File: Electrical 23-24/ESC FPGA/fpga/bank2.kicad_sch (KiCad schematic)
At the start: 1 part, among them U1 XC6SLX4-TQG144

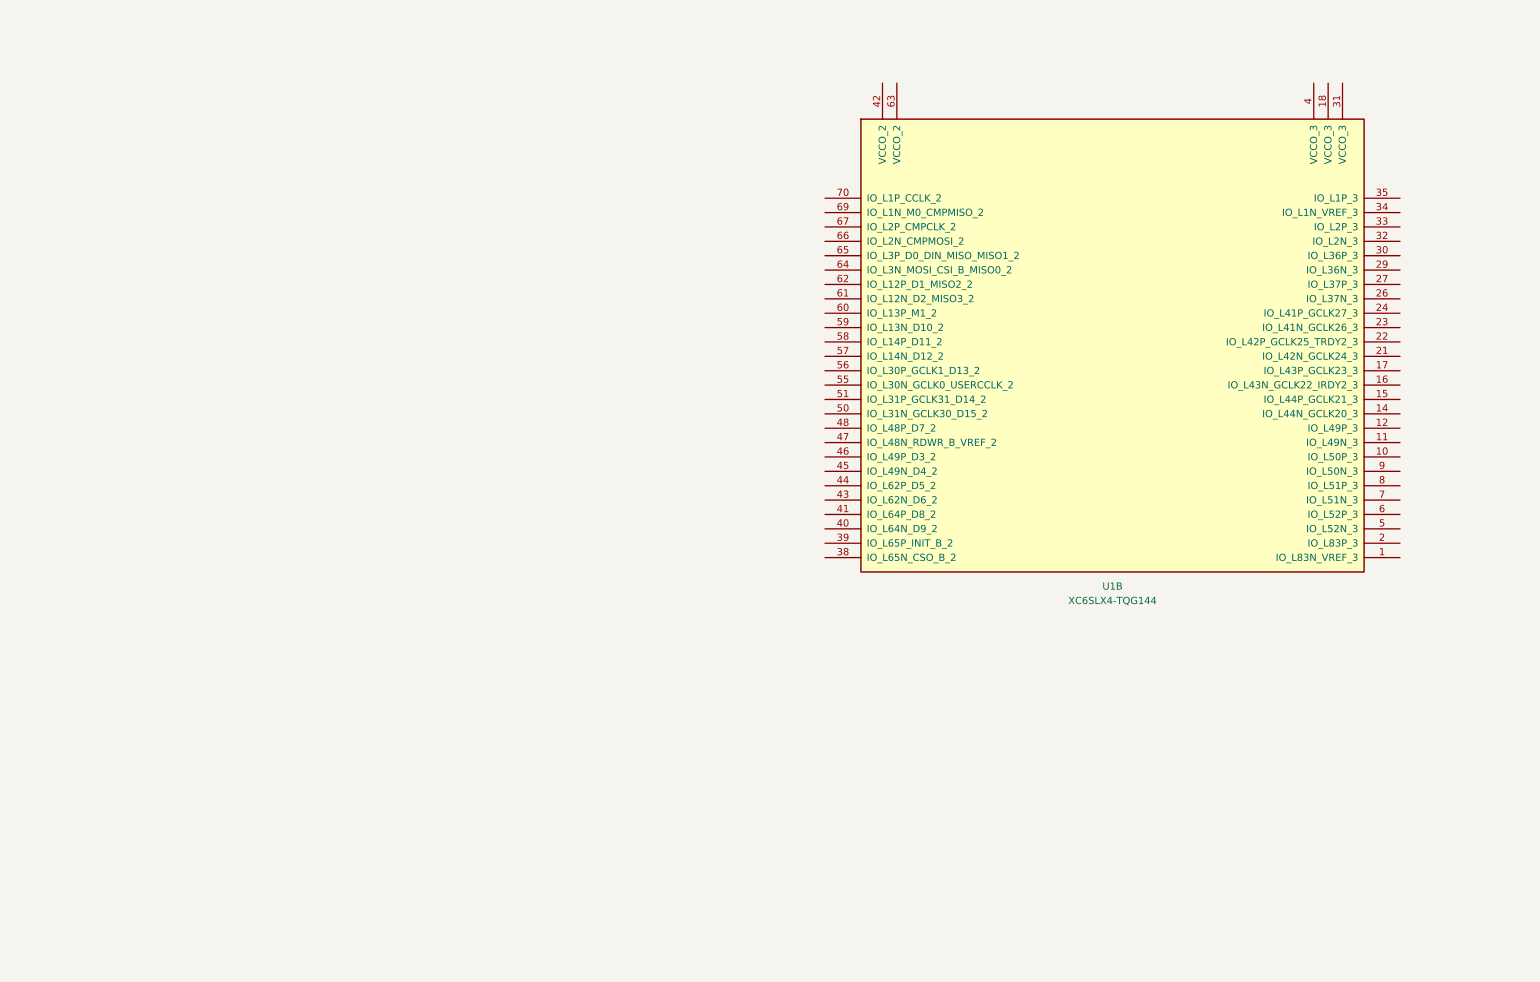
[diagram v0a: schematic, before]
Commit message: Finish programming interface with FPGA
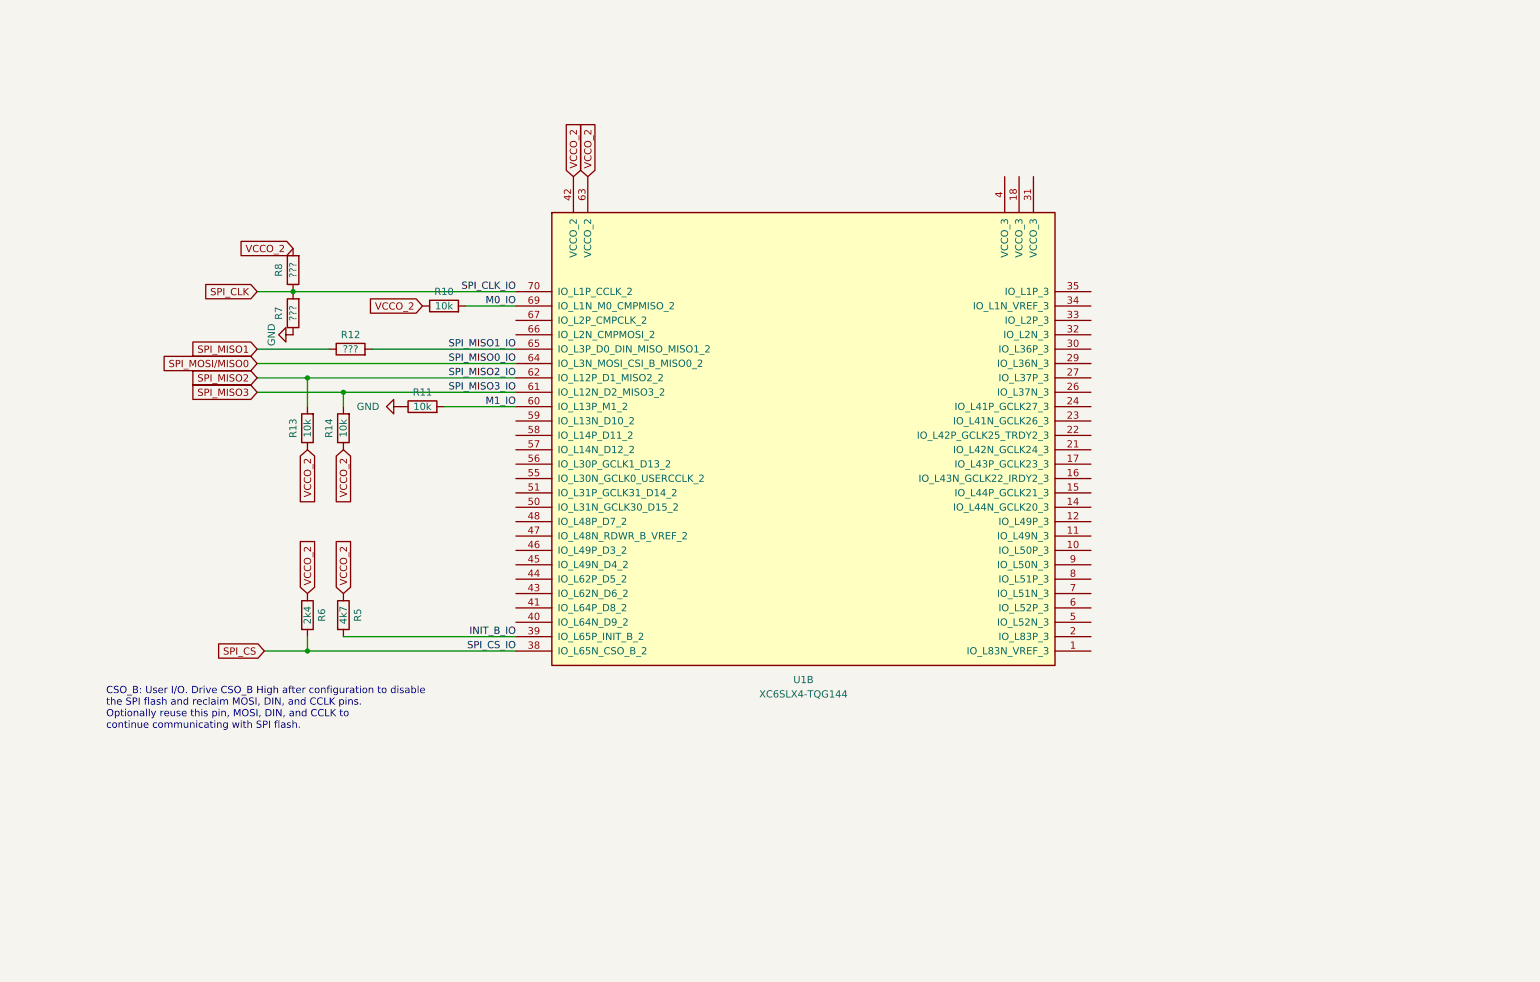
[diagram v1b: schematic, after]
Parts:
- added R10, R11, R13, R14: 10k, symbol Device:R
- added R12, R7, R8: ???, symbol Device:R
- added R5: 4k7, symbol Device:R
- added R6: 2k4, symbol Device:R
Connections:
- net SPI_CS: now reaches U1.38 (IO_L65N_CSO_B_2)
- net SPI_CS: now also R6.2
- net INIT_B_IO: now reaches U1.39 (IO_L65P_INIT_B_2)
- net INIT_B_IO: now also R5.2
- net VCCO_2: now reaches U1.42 (VCCO_2)
- net VCCO_2: now also U1.63 (VCCO_2), R10.1, R13.1, R14.1, R5.1, R6.1, R8.2
- net M1_IO: now reaches U1.60 (IO_L13P_M1_2)
- net M1_IO: now also R11.2
- net SPI_MISO3: now reaches U1.61 (IO_L12N_D2_MISO3_2)
- net SPI_MISO3: now also R14.2
- net SPI_MISO2: now reaches U1.62 (IO_L12P_D1_MISO2_2)
- net SPI_MISO2: now also R13.2
- net SPI_MOSI/MISO0: now reaches U1.64 (IO_L3N_MOSI_CSI_B_MISO0_2)
- net SPI_MISO1_IO: now reaches U1.65 (IO_L3P_D0_DIN_MISO_MISO1_2)
- net SPI_MISO1_IO: now also R12.2
- net M0_IO: now reaches U1.69 (IO_L1N_M0_CMPMISO_2)
- net M0_IO: now also R10.2
- net SPI_CLK: now reaches U1.70 (IO_L1P_CCLK_2)
- net SPI_CLK: now also R7.2, R8.1
- new net GND: R11.1, R7.1
- new net SPI_MISO1: R12.1
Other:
- note added: "CSO_B: User I/O. Drive CSO_B High after configuration to disable the SPI flash and reclaim MOSI, DIN, and CCLK pins. Optionally reuse this pin, MOSI, DIN, and CCLK to continue communicating with SPI flash."
- moved on the sheet: U1B

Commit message: idk but something
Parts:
- added C6 (x4): u47, symbol Device:C
- added C6 (x2): 4u7, symbol Device:C
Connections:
- net GND: now also C6.2, C6.2, C6.2, C6.2, C6.2, C6.2
- net VCCO_2: now also C6.1, C6.1, C6.1
- net VCCO_3: now reaches U1.18 (VCCO_3)
- net VCCO_3: now also U1.31 (VCCO_3), U1.4 (VCCO_3), C6.1, C6.1, C6.1
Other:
- note added: "why is this resistor"

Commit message: DR Feedback
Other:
- note added: "4 pmod 8 switches (dip switch) gpio (raspi header or arduino shield) rgb led 1 led per button level shifter? HDMI"
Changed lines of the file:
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@@
+    (effects (font (size 1.27 1.27)) (justify left bottom))
+  )
+  (text "4 pmod\n8 switches (dip switch)\ngpio (raspi header or arduino shield)\nrgb led\n1 led per button\nlevel shifter?\nHDMI"
+    (at 214.63 105.41 0)
     (effects (font (size 1.27 1.27)) (justify left bottom))
   )

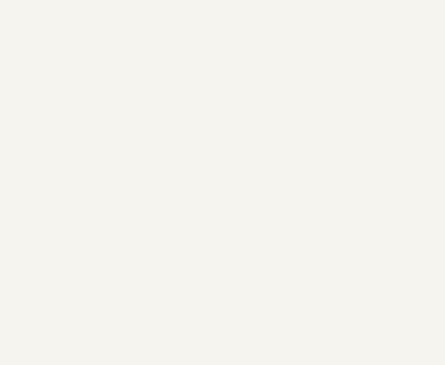
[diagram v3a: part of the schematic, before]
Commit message: Add fpga stuff and stencils
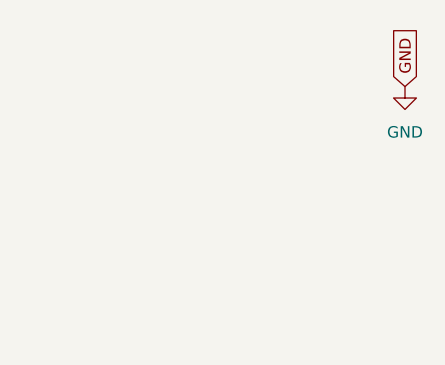
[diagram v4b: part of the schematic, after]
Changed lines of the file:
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@@
+    )
+  )
+  (global_label "GND" (shape input) (at 271.78 30.48 90) (fields_autoplaced)
+    (effects (font (size 1.27 1.27)) (justify left))
+    (property "Intersheetrefs" "${INTERSHEET_REFS}" (at 271.78 23.6243 90)
+      (effects (font (size 1.27 1.27)) (justify left) hide)
     )
   )
@@
         )
       )
+    )
+  )
+  (symbol (lib_id "power:GND") (at 271.78 30.48 0) (unit 1)
+    (in_bom yes) (on_board yes) (dnp no) (fields_autoplaced)
+    (property "Reference" "#PWR016" (at 271.78 36.83 0)
+      (effects (font (size 1.27 1.27)) hide)
+    )
+    (property "Value" "GND" (at 271.78 35.56 0)
+      (effects (font (size 1.27 1.27)))
+    )
+    (property "Footprint" "" (at 271.78 30.48 0)
+      (effects (font (size 1.27 1.27)) hide)
+    )
+    (property "Datasheet" "" (at 271.78 30.48 0)
+      (effects (font (size 1.27 1.27)) hide)
+    )
+    (pin "1")
+    (instances
+      (project "fpga"
+        (path "/5bf59577-a814-4364-8f7a-37815cfb5474/3e04db34-3f8a-4742-be82-6fa24c009343"
+          (reference "#PWR016") (unit 1)
+        )
+        (path "/5bf59577-a814-4364-8f7a-37815cfb5474/1f83b38b-56ef-4110-879b-13379f9dd920"
+          (reference "#PWR026") (unit 1)
+        )
+        (path "/5bf59577-a814-4364-8f7a-37815cfb5474/a286b274-4434-47ab-983d-e64806fdcbd6"
+          (reference "#PWR036") (unit 1)
+        )
+      )

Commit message: Working on FPGA board
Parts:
- added C52: 0.01uF, Capacitor_SMD:C_0603_1608Metric_Pad1.08x0.95mm_HandSolder, symbol Device:C_Small
- added X1: KC5032Z100.000C1JX00, Oscillator:Oscillator_SMD_EuroQuartz_XO53-4Pin_5.0x3.2mm_HandSoldering, symbol Oscillator:ASE-xxxMHz
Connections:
- net GND: now also C52.1, X1.2 (GND)
- net OSCI: now reaches U1.55 (IO_L30N_GCLK0_USERCCLK_2)
- net OSCI: now also X1.3 (OUT)
- new net 3V3: C52.2, X1.1 (EN), X1.4 (Vdd)
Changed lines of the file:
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@@
+    (stroke (width 0) (type default))
+  )
+  (wire (pts (xy 55.88 170.18) (xy 59.69 170.18))
     (stroke (width 0) (type default))
   )
@@
     (effects (font (size 1.27 1.27)) (justify right bottom))
   )
+  (label "OSCI" (at 104.14 104.14 180) (fields_autoplaced)
+    (effects (font (size 1.27 1.27)) (justify right bottom))
+  )
   (label "M1_IO" (at 104.14 91.44 180) (fields_autoplaced)
     (effects (font (size 1.27 1.27)) (justify right bottom))
@@
     (effects (font (size 1.27 1.27)) (justify right bottom))
   )
+  (label "OSCI" (at 67.31 177.8 0) (fields_autoplaced)
+    (effects (font (size 1.27 1.27)) (justify left bottom))
+  )
   (label "SPI_MISO2_IO" (at 104.14 86.36 180) (fields_autoplaced)
     (effects (font (size 1.27 1.27)) (justify right bottom))
@@
     (property "Intersheetrefs" "${INTERSHEET_REFS}" (at 77.5086 73.66 0)
       (effects (font (size 1.27 1.27)) (justify right) hide)
+    )
+  )
+  (global_label "3V3" (shape input) (at 52.07 177.8 180) (fields_autoplaced)
+    (effects (font (size 1.27 1.27)) (justify right))
+    (property "Intersheetrefs" "${INTERSHEET_REFS}" (at 45.5772 177.8 0)
+      (effects (font (size 1.27 1.27)) (justify right) hide)
+    )
+  )
+  (global_label "3V3" (shape input) (at 59.69 170.18 90) (fields_autoplaced)
+    (effects (font (size 1.27 1.27)) (justify left))
+    (property "Intersheetrefs" "${INTERSHEET_REFS}" (at 59.69 163.6872 90)
+      (effects (font (size 1.27 1.27)) (justify left) hide)
     )
   )
@@
     )
   )
+  (symbol (lib_id "power:GND") (at 59.69 185.42 0) (unit 1)
+    (in_bom yes) (on_board yes) (dnp no)
+    (property "Reference" "#PWR092" (at 59.69 191.77 0)
+      (effects (font (size 1.27 1.27)) hide)
+    )
+    (property "Value" "GND" (at 59.817 189.8142 0)
+      (effects (font (size 1.27 1.27)))
+    )
+    (property "Footprint" "" (at 59.69 185.42 0)
+      (effects (font (size 1.27 1.27)) hide)
+    )
+    (property "Datasheet" "" (at 59.69 185.42 0)
+      (effects (font (size 1.27 1.27)) hide)
+    )
+    (pin "1")
+    (instances
+      (project "fpga"
+        (path "/5bf59577-a814-4364-8f7a-37815cfb5474/a286b274-4434-47ab-983d-e64806fdcbd6"
+          (reference "#PWR092") (unit 1)
+        )
+      )
+      (project "programmer"
+        (path "/aaaf4408-e4eb-45ee-a27d-c2b42f2a1569/1155aff1-def4-4854-ae66-7f7d5ef155d7"
+          (reference "#PWR024") (unit 1)
+        )
+      )
+      (project "JTAG_HW"
+        (path "/c86165a3-b3de-4c2c-b13d-de333b5047c7"
+          (reference "#PWR02") (unit 1)
+        )
+      )
+    )
+  )
   (symbol (lib_id "power:GND") (at 83.82 91.44 270) (unit 1)
     (in_bom yes) (on_board yes) (dnp no) (fields_autoplaced)
@@
     )
   )
+  (symbol (lib_id "Oscillator:ASE-xxxMHz") (at 59.69 177.8 0) (unit 1)
+    (in_bom yes) (on_board yes) (dnp no)
+    (property "Reference" "X1" (at 43.18 181.7721 0)
+      (effects (font (size 1.27 1.27)))
+    )
+    (property "Value" "KC5032Z100.000C1JX00" (at 43.18 184.15 0)
+      (effects (font (size 1.27 1.27)))
+    )
+    (property "Footprint" "Oscillator:Oscillator_SMD_EuroQuartz_XO53-4Pin_5.0x3.2mm_HandSoldering" (at 77.47 186.69 0)
+      (effects (font (size 1.27 1.27)) hide)
+    )
+    (property "Datasheet" "https://mm.digikey.com/Volume0/opasdata/d220001/medias/docus/5791/KC5032Z.pdf" (at 57.15 177.8 0)
+      (effects (font (size 1.27 1.27)) hide)
+    )
+    (property "Digi" "https://www.digikey.com/en/products/detail/kyocera-avx/KC5032Z100-000C1JX00/22205198" (at 59.69 177.8 0)
+      (effects (font (size 1.27 1.27)) hide)
+    )
+    (pin "1")
+    (pin "2")
+    (pin "3")
+    (pin "4")
+    (instances
+      (project "fpga"
+        (path "/5bf59577-a814-4364-8f7a-37815cfb5474/a286b274-4434-47ab-983d-e64806fdcbd6"
+          (reference "X1") (unit 1)
+        )
+      )
+      (project "programmer"
+        (path "/aaaf4408-e4eb-45ee-a27d-c2b42f2a1569/1155aff1-def4-4854-ae66-7f7d5ef155d7"
+          (reference "X1") (unit 1)
+        )
+      )
+    )
+  )
   (symbol (lib_id "Device:C") (at 210.82 46.99 0) (unit 1)
     (in_bom yes) (on_board yes) (dnp no)
@@
     )
   )
+  (symbol (lib_id "Device:C_Small") (at 53.34 170.18 90) (unit 1)
+    (in_bom yes) (on_board yes) (dnp no)
+    (property "Reference" "C52" (at 54.737 167.259 90)
+      (effects (font (size 1.27 1.27)) (justify left))
+    )
+    (property "Value" "0.01uF" (at 55.88 165.1 90)
+      (effects (font (size 1.27 1.27)) (justify left))
+    )
+    (property "Footprint" "Capacitor_SMD:C_0603_1608Metric_Pad1.08x0.95mm_HandSolder" (at 53.34 170.18 0)
+      (effects (font (size 1.27 1.27)) hide)
+    )
+    (property "Datasheet" "~" (at 53.34 170.18 0)
+      (effects (font (size 1.27 1.27)) hide)
+    )
+    (pin "1")
+    (pin "2")
+    (instances
+      (project "fpga"
+        (path "/5bf59577-a814-4364-8f7a-37815cfb5474/a286b274-4434-47ab-983d-e64806fdcbd6"
+          (reference "C52") (unit 1)
+        )
+      )
+      (project "programmer"
+        (path "/aaaf4408-e4eb-45ee-a27d-c2b42f2a1569/1155aff1-def4-4854-ae66-7f7d5ef155d7"
+          (reference "C4") (unit 1)
+        )
+      )
+      (project "JTAG_HW"
+        (path "/c86165a3-b3de-4c2c-b13d-de333b5047c7"
+          (reference "C4") (unit 1)
+        )
+      )
+    )
+  )
   (symbol (lib_id "Device:C") (at 121.92 46.99 0) (unit 1)
     (in_bom yes) (on_board yes) (dnp no)
@@
         )
       )
+    )
+  )
+  (symbol (lib_id "power:GND") (at 50.8 170.18 270) (unit 1)
+    (in_bom yes) (on_board yes) (dnp no)
+    (property "Reference" "#PWR089" (at 44.45 170.18 0)
+      (effects (font (size 1.27 1.27)) hide)
+    )
+    (property "Value" "GND" (at 46.4058 170.307 0)
+      (effects (font (size 1.27 1.27)))
+    )
+    (property "Footprint" "" (at 50.8 170.18 0)
+      (effects (font (size 1.27 1.27)) hide)
+    )
+    (property "Datasheet" "" (at 50.8 170.18 0)
+      (effects (font (size 1.27 1.27)) hide)
+    )
+    (pin "1")
+    (instances
+      (project "fpga"
+        (path "/5bf59577-a814-4364-8f7a-37815cfb5474/a286b274-4434-47ab-983d-e64806fdcbd6"
+          (reference "#PWR089") (unit 1)
+        )
+      )
+      (project "programmer"
+        (path "/aaaf4408-e4eb-45ee-a27d-c2b42f2a1569/1155aff1-def4-4854-ae66-7f7d5ef155d7"
+          (reference "#PWR022") (unit 1)
+        )
+      )
+      (project "JTAG_HW"
+        (path "/c86165a3-b3de-4c2c-b13d-de333b5047c7"
+          (reference "#PWR02") (unit 1)
+        )
+      )

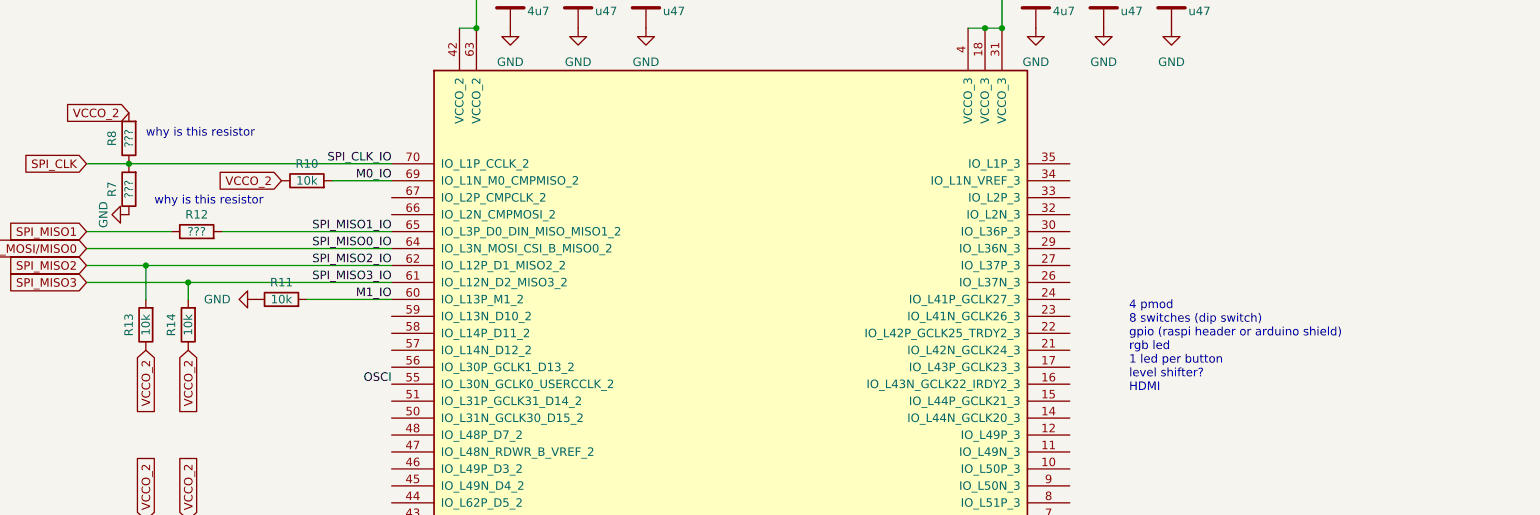
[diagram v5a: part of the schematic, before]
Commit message: Add level shifters
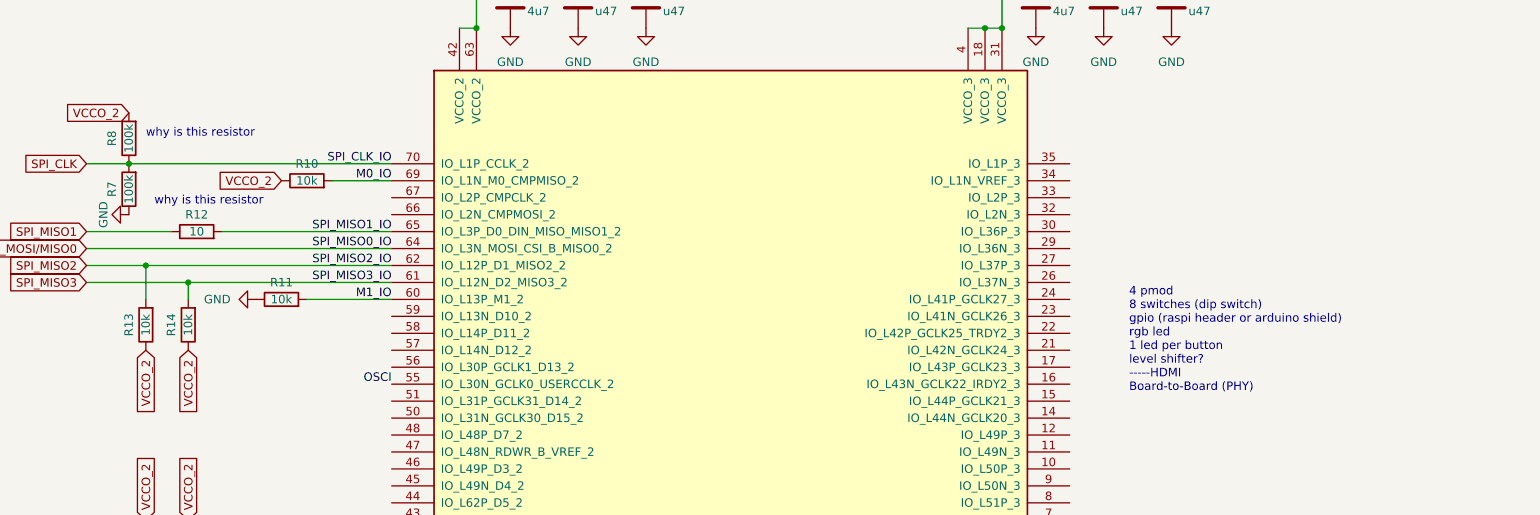
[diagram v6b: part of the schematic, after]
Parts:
- R12: value ??? -> 10
- R7, R8: value ??? -> 100k
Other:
- note added: "4 pmod 8 switches (dip switch) gpio (raspi header or arduino shield) rgb led 1 led per button level shifter? -----HDMI Board-to-Board (PHY)"
- note removed: "4 pmod 8 switches (dip switch) gpio (raspi header or arduino shield) rgb led 1 led per button level shifter? HDMI"
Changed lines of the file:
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@@
     (effects (font (size 1.27 1.27)) (justify left bottom))
   )
-  (text "4 pmod\n8 switches (dip switch)\ngpio (raspi header or arduino shield)\nrgb led\n1 led per button\nlevel shifter?\nHDMI"
+  (text "4 pmod\n8 switches (dip switch)\ngpio (raspi header or arduino shield)\nrgb led\n1 led per button\nlevel shifter?\n-----HDMI\nBoard-to-Board (PHY)"
     (at 214.63 105.41 0)
     (effects (font (size 1.27 1.27)) (justify left bottom))
@@
       (effects (font (size 1.27 1.27)))
     )
-    (property "Value" "???" (at 74.93 81.28 90)
+    (property "Value" "10" (at 74.93 81.28 90)
       (effects (font (size 1.27 1.27)))
     )
@@
       (effects (font (size 1.27 1.27)))
     )
-    (property "Value" "???" (at 64.77 74.93 90)
+    (property "Value" "100k" (at 64.77 74.93 90)
       (effects (font (size 1.27 1.27)))
     )
@@
       (effects (font (size 1.27 1.27)))
     )
-    (property "Value" "???" (at 64.77 67.31 90)
-      (effects (font (size 1.27 1.27)))
-    )
+    (property "Value" "100k" (at 64.77 67.31 90)
+      (effects (font (size 1.27 1.27)))
+    )
